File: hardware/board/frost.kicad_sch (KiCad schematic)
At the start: 0 parts

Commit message: reading up on power
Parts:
- added U1: RK3568, RK3568:BGA636C65P28X28_1900X1900X168, symbol RK3568:RK3568
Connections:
- new net AVSS1: U1.J27 (AVSS1), U1.L24 (AVSS1), U1.L26 (AVSS1), U1.M21 (AVSS1), U1.M26 (AVSS1), U1.N28 (AVSS1), U1.P21 (AVSS1), U1.P26 (AVSS1), U1.R23 (AVSS1), U1.R26 (AVSS1), U1.U23 (AVSS1), U1.U26 (AVSS1), U1.V14 (AVSS1), U1.V15 (AVSS1), U1.V16 (AVSS1)
- new net AVSS2: U1.AA12 (AVSS2), U1.AA14 (AVSS2), U1.AA15 (AVSS2), U1.AA17 (AVSS2), U1.AA24 (AVSS2), U1.AA26 (AVSS2), U1.AB11 (AVSS2), U1.V22 (AVSS2), U1.V23 (AVSS2), U1.V26 (AVSS2), U1.W17 (AVSS2), U1.Y18 (AVSS2), U1.Y23 (AVSS2), U1.Y24 (AVSS2), U1.Y26 (AVSS2)
- new net AVSS3: U1.AB12 (AVSS3), U1.AB14 (AVSS3), U1.AB15 (AVSS3), U1.AB17 (AVSS3), U1.AC11 (AVSS3), U1.AC12 (AVSS3), U1.AC15 (AVSS3), U1.AC18 (AVSS3), U1.AC25 (AVSS3), U1.AC26 (AVSS3), U1.AC9 (AVSS3), U1.AD26 (AVSS3), U1.AE14 (AVSS3), U1.AE17 (AVSS3), U1.AE20 (AVSS3)
- new net AVSS4: U1.AE27 (AVSS4), U1.AE28 (AVSS4), U1.AF11 (AVSS4), U1.AF12 (AVSS4), U1.AF14 (AVSS4), U1.AF15 (AVSS4), U1.AF17 (AVSS4), U1.AF18 (AVSS4), U1.AF20 (AVSS4), U1.AF21 (AVSS4), U1.AF9 (AVSS4), U1.AG18 (AVSS4), U1.AH18 (AVSS4), U1.AH23 (AVSS4)
- new net DDRPHY_VDDQ: U1.H11 (DDRPHY_VDDQ), U1.H12 (DDRPHY_VDDQ), U1.H14 (DDRPHY_VDDQ), U1.H15 (DDRPHY_VDDQ), U1.H9 (DDRPHY_VDDQ), U1.J9 (DDRPHY_VDDQ), U1.L9 (DDRPHY_VDDQ), U1.M9 (DDRPHY_VDDQ)
- new net DDRPHY_VDDQL: U1.J11 (DDRPHY_VDDQL), U1.J12 (DDRPHY_VDDQL), U1.J14 (DDRPHY_VDDQL), U1.K10 (DDRPHY_VDDQL), U1.L10 (DDRPHY_VDDQL), U1.M10 (DDRPHY_VDDQL)
- new net MULTI_PHY_AVDD_0V9: U1.R20 (MULTI_PHY_AVDD_0V9), U1.R21 (MULTI_PHY_AVDD_0V9)
- new net PCIE30_AVDD_0V9: U1.U20 (PCIE30_AVDD_0V9), U1.U21 (PCIE30_AVDD_0V9)
- new net VCCIO5: U1.V10 (VCCIO5), U1.V11 (VCCIO5)
- new net VCCIO6: U1.R9 (VCCIO6), U1.U9 (VCCIO6)
- new net VDD_CPU: U1.J15 (VDD_CPU), U1.K15 (VDD_CPU), U1.K16 (VDD_CPU), U1.K17 (VDD_CPU), U1.K18 (VDD_CPU), U1.L15 (VDD_CPU), U1.L16 (VDD_CPU), U1.L17 (VDD_CPU), U1.L18 (VDD_CPU), U1.M17 (VDD_CPU)
- new net VDD_GPU: U1.R13 (VDD_GPU), U1.T13 (VDD_GPU), U1.U11 (VDD_GPU), U1.U12 (VDD_GPU), U1.U13 (VDD_GPU)
- new net VDD_LOGIC: U1.L12 (VDD_LOGIC), U1.M12 (VDD_LOGIC), U1.N13 (VDD_LOGIC), U1.N16 (VDD_LOGIC), U1.P13 (VDD_LOGIC), U1.P16 (VDD_LOGIC), U1.R12 (VDD_LOGIC), U1.R16 (VDD_LOGIC), U1.T12 (VDD_LOGIC), U1.T16 (VDD_LOGIC)
- new net VDD_NPU: U1.M19 (VDD_NPU), U1.N19 (VDD_NPU), U1.P18 (VDD_NPU), U1.P19 (VDD_NPU), U1.P20 (VDD_NPU)
- new net VSS1: U1.A1 (VSS1), U1.A10 (VSS1), U1.A14 (VSS1), U1.A18 (VSS1), U1.A28 (VSS1), U1.A3 (VSS1), U1.A6 (VSS1), U1.B12 (VSS1), U1.B16 (VSS1), U1.B23 (VSS1), U1.B26 (VSS1), U1.B5 (VSS1), U1.B9 (VSS1), U1.C3 (VSS1), U1.C6 (VSS1)
- new net VSS10: U1.AB2 (VSS10), U1.AB6 (VSS10), U1.AD3 (VSS10), U1.AE21 (VSS10), U1.AE6 (VSS10), U1.AF26 (VSS10), U1.AF3 (VSS10), U1.AG5 (VSS10), U1.AH1 (VSS10), U1.AH28 (VSS10), U1.AH8 (VSS10)
- new net VSS2: U1.C11 (VSS2), U1.C12 (VSS2), U1.C14 (VSS2), U1.C15 (VSS2), U1.C17 (VSS2), U1.C18 (VSS2), U1.C25 (VSS2), U1.C8 (VSS2), U1.C9 (VSS2), U1.D11 (VSS2), U1.D2 (VSS2), U1.D28 (VSS2), U1.D3 (VSS2), U1.E3 (VSS2), U1.E7 (VSS2)
- new net VSS3: U1.F1 (VSS3), U1.F12 (VSS3), U1.F14 (VSS3), U1.F15 (VSS3), U1.F17 (VSS3), U1.F3 (VSS3), U1.F9 (VSS3), U1.G11 (VSS3), U1.G12 (VSS3), U1.G14 (VSS3), U1.G15 (VSS3), U1.G5 (VSS3), U1.G6 (VSS3), U1.G8 (VSS3), U1.G9 (VSS3)
- new net VSS4: U1.G17 (VSS4), U1.G18 (VSS4), U1.G24 (VSS4), U1.H2 (VSS4), U1.H3 (VSS4), U1.H6 (VSS4), U1.J17 (VSS4), U1.J18 (VSS4), U1.J20 (VSS4), U1.J22 (VSS4), U1.J26 (VSS4), U1.J3 (VSS4), U1.J5 (VSS4), U1.K1 (VSS4), U1.K11 (VSS4)
- new net VSS5: U1.K12 (VSS5), U1.K13 (VSS5), U1.K14 (VSS5), U1.K19 (VSS5), U1.L11 (VSS5), U1.L13 (VSS5), U1.L14 (VSS5), U1.L19 (VSS5), U1.L20 (VSS5), U1.L21 (VSS5), U1.L3 (VSS5), U1.L5 (VSS5), U1.L8 (VSS5), U1.M2 (VSS5), U1.M3 (VSS5)
- new net VSS6: U1.M11 (VSS6), U1.M13 (VSS6), U1.M14 (VSS6), U1.M16 (VSS6), U1.M18 (VSS6), U1.M6 (VSS6), U1.M8 (VSS6), U1.N1 (VSS6), U1.N12 (VSS6), U1.N14 (VSS6), U1.N15 (VSS6), U1.N17 (VSS6), U1.N18 (VSS6), U1.P3 (VSS6), U1.P6 (VSS6)
- new net VSS7: U1.P12 (VSS7), U1.P14 (VSS7), U1.P15 (VSS7), U1.P17 (VSS7), U1.R10 (VSS7), U1.R11 (VSS7), U1.R14 (VSS7), U1.R15 (VSS7), U1.R17 (VSS7), U1.R18 (VSS7), U1.R19 (VSS7), U1.R3 (VSS7), U1.R6 (VSS7), U1.T10 (VSS7), U1.T11 (VSS7)
- new net VSS8: U1.T14 (VSS8), U1.T15 (VSS8), U1.T17 (VSS8), U1.T18 (VSS8), U1.T19 (VSS8), U1.U1 (VSS8), U1.U10 (VSS8), U1.U14 (VSS8), U1.U15 (VSS8), U1.U16 (VSS8), U1.U17 (VSS8), U1.U18 (VSS8), U1.U6 (VSS8), U1.U7 (VSS8), U1.U8 (VSS8)
- new net VSS9: U1.AA23 (VSS9), U1.AA4 (VSS9), U1.AA9 (VSS9), U1.V13 (VSS9), U1.V3 (VSS9), U1.V8 (VSS9), U1.V9 (VSS9), U1.W10 (VSS9), U1.W11 (VSS9), U1.W12 (VSS9), U1.W13 (VSS9), U1.Y11 (VSS9), U1.Y12 (VSS9), U1.Y8 (VSS9), U1.Y9 (VSS9)
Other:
- added sheet Ethernet (ethernet.kicad_sch)
- added sheet HDMI (hdmi.kicad_sch)
- added sheet Memory and Storage (memory_storage.kicad_sch)
- added sheet Peripherals (peripherals.kicad_sch)
- added sheet Power (power.kicad_sch)
- added sheet USB (usb.kicad_sch)
- added sheet WiFi and Bluetooth (wireless.kicad_sch)

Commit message: emmc stuff
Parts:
- U1: LCSC (none) -> C3345225
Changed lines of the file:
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@@
 			)
 		)
+		(property "LCSC" "C3345225"
+			(at 52.07 113.03 0)
+			(effects
+				(font
+					(size 1.27 1.27)
+				)
+				(hide yes)
+			)
+		)
 		(pin "D26"
 		)
@@
 			)
 		)
+		(property "LCSC" "C3345225"
+			(at -208.28 295.91 0)
+			(effects
+				(font
+					(size 1.27 1.27)
+				)
+				(hide yes)
+			)
+		)
 		(pin "D26"
 		)
@@
 			)
 		)
+		(property "LCSC" "C3345225"
+			(at 304.8 344.17 0)
+			(effects
+				(font
+					(size 1.27 1.27)
+				)
+				(hide yes)
+			)
+		)
 		(pin "D26"
 		)
@@
 			)
 		)
+		(property "LCSC" "C3345225"
+			(at -30.48 391.16 0)
+			(effects
+				(font
+					(size 1.27 1.27)
+				)
+				(hide yes)
+			)
+		)
 		(pin "D26"
 		)
@@
 			)
 		)
+		(property "LCSC" "C3345225"
+			(at -224.79 99.06 0)
+			(effects
+				(font
+					(size 1.27 1.27)
+				)
+				(hide yes)
+			)
+		)
 		(pin "D26"
 		)
@@
 			)
 		)
+		(property "LCSC" "C3345225"
+			(at 45.72 144.78 0)
+			(effects
+				(font
+					(size 1.27 1.27)
+				)
+				(hide yes)
+			)
+		)
 		(pin "D26"
 		)
@@
 			)
 		)
+		(property "LCSC" "C3345225"
+			(at -147.32 463.55 0)
+			(effects
+				(font
+					(size 1.27 1.27)
+				)
+				(hide yes)
+			)
+		)
 		(pin "D26"
 		)
@@
 			)
 		)
+		(property "LCSC" "C3345225"
+			(at -55.88 87.63 0)
+			(effects
+				(font
+					(size 1.27 1.27)
+				)
+				(hide yes)
+			)
+		)
 		(pin "D26"
 		)
@@
 			)
 		)
+		(property "LCSC" "C3345225"
+			(at 328.93 219.71 0)
+			(effects
+				(font
+					(size 1.27 1.27)
+				)
+				(hide yes)
+			)
+		)
 		(pin "D26"
 		)
@@
 			)
 		)
+		(property "LCSC" "C3345225"
+			(at 242.57 367.03 0)
+			(effects
+				(font
+					(size 1.27 1.27)
+				)
+				(hide yes)
+			)
+		)
 		(pin "D26"
 		)
@@
 			)
 		)
+		(property "LCSC" "C3345225"
+			(at -152.4 361.95 0)
+			(effects
+				(font
+					(size 1.27 1.27)
+				)
+				(hide yes)
+			)
+		)
 		(pin "D26"
 		)
@@
 			)
 		)
+		(property "LCSC" "C3345225"
+			(at -363.22 251.46 0)
+			(effects
+				(font
+					(size 1.27 1.27)
+				)
+				(hide yes)
+			)
+		)
 		(pin "D26"
 		)
@@
 			)
 		)
+		(property "LCSC" "C3345225"
+			(at 55.88 72.39 0)
+			(effects
+				(font
+					(size 1.27 1.27)
+				)
+				(hide yes)
+			)
+		)
 		(pin "D26"
 		)
@@
 			)
 		)
+		(property "LCSC" "C3345225"
+			(at -279.4 445.77 0)
+			(effects
+				(font
+					(size 1.27 1.27)
+				)
+				(hide yes)
+			)
+		)
 		(pin "D26"
 		)
@@
 			)
 		)
+		(property "LCSC" "C3345225"
+			(at 33.02 307.34 0)
+			(effects
+				(font
+					(size 1.27 1.27)
+				)
+				(hide yes)
+			)
+		)
 		(pin "D26"
 		)
@@
 			)
 		)
+		(property "LCSC" "C3345225"
+			(at 121.92 314.96 0)
+			(effects
+				(font
+					(size 1.27 1.27)
+				)
+				(hide yes)
+			)
+		)
 		(pin "D26"
 		)
@@
 			)
 		)
+		(property "LCSC" "C3345225"
+			(at 200.66 308.61 0)
+			(effects
+				(font
+					(size 1.27 1.27)
+				)
+				(hide yes)
+			)
+		)
 		(pin "D26"
 		)
@@
 			)
 		)
+		(property "LCSC" "C3345225"
+			(at -359.41 153.67 0)
+			(effects
+				(font
+					(size 1.27 1.27)
+				)
+				(hide yes)
+			)
+		)
 		(pin "D26"
 		)
@@
 				(hide yes)
 			)
+		)
+		(property "LCSC" "C3345225"
+			(at -331.47 342.9 0)
+			(effects
+				(font
+					(size 1.27 1.27)
+				)
+				(hide yes)
+			)

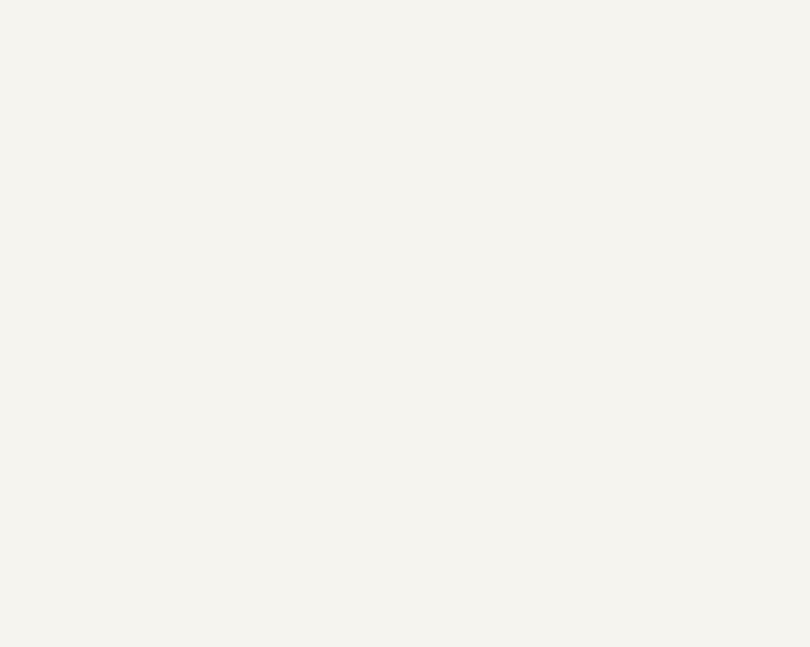
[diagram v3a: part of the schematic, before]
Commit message: MIPI IS FAKE
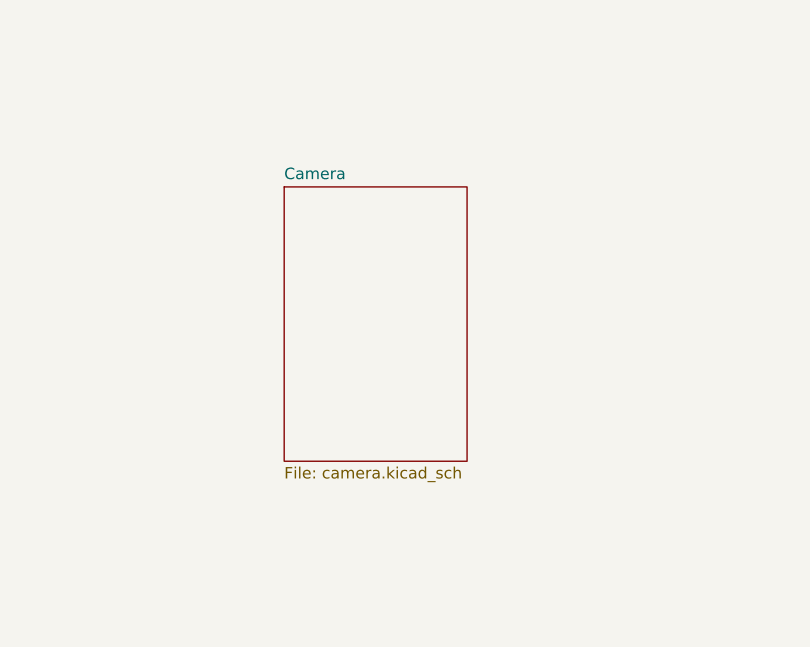
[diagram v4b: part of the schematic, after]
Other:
- added sheet Camera (camera.kicad_sch)
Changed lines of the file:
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@@
+		)
+	)
+	(sheet
+		(at 251.46 85.09)
+		(size 20.32 30.48)
+		(exclude_from_sim no)
+		(in_bom yes)
+		(on_board yes)
+		(dnp no)
+		(fields_autoplaced yes)
+		(stroke
+			(width 0.1524)
+			(type solid)
+		)
+		(fill
+			(color 0 0 0 0.0000)
+		)
+		(property "Sheetname" "Camera"
+			(at 251.46 84.3784 0)
+			(effects
+				(font
+					(size 1.27 1.27)
+				)
+				(justify left bottom)
+			)
+		)
+		(property "Sheetfile" "camera.kicad_sch"
+			(at 251.46 116.1546 0)
+			(effects
+				(font
+					(size 1.27 1.27)
+				)
+				(justify left top)
+			)
+		)
+		(instances
+			(project "frost"
+				(path "/3bc38516-4fe0-4022-adb8-9fd55b66cd2d"
+					(page "9")
+				)
+			)
 		)
 	)

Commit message: start of ethernet
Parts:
- removed unit 13 of U1
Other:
- added sheet Display (display.kicad_sch)

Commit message: add in pcie and ddr4
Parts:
- removed unit 2 of U1
- removed unit 3 of U1
- removed unit 4 of U1
- removed unit 1 of U1
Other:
- added sheet PCIE (pcie.kicad_sch)

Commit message: sensors
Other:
- added sheet Sensors (sensors.kicad_sch)
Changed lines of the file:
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@@
+	)
+	(sheet
+		(at 396.24 398.78)
+		(size 73.66 52.07)
+		(exclude_from_sim no)
+		(in_bom yes)
+		(on_board yes)
+		(dnp no)
+		(fields_autoplaced yes)
+		(stroke
+			(width 0.1524)
+			(type solid)
+		)
+		(fill
+			(color 0 0 0 0.0000)
+		)
+		(property "Sheetname" "Sensors"
+			(at 396.24 398.0684 0)
+			(effects
+				(font
+					(size 1.27 1.27)
+				)
+				(justify left bottom)
+			)
+		)
+		(property "Sheetfile" "sensors.kicad_sch"
+			(at 396.24 451.4346 0)
+			(effects
+				(font
+					(size 1.27 1.27)
+				)
+				(justify left top)
+			)
+		)
+		(instances
+			(project "frost"
+				(path "/3bc38516-4fe0-4022-adb8-9fd55b66cd2d"
+					(page "12")
+				)
+			)
+		)
 	)
 	(sheet

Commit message: finished schematic!
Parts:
- removed unit 15 of U1
- removed unit 10 of U1
- removed unit 17 of U1
- removed unit 22 of U1
- removed unit 11 of U1
- removed unit 12 of U1
- removed unit 14 of U1
- removed unit 21 of U1
- removed unit 7 of U1
- removed unit 8 of U1
- removed unit 9 of U1
- removed unit 20 of U1
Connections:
- no-connect marks 0 -> 24
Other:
- moved on the sheet: U1R, U1S
